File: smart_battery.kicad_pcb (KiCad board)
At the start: 4 copper layers, 50 x 18 mm, 98 parts, among them J101 Conn_01x02_Male, J102 Conn_01x02_Male, J103 Conn_01x05_Male, J104 Dronecode_Debug, Q101 RZM001P02T2L, Q201 PMGD280UN,115, Q202 PMGD280UN,115, U101 NCP716, U102 STM32F051K6Ux, U103 INA181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

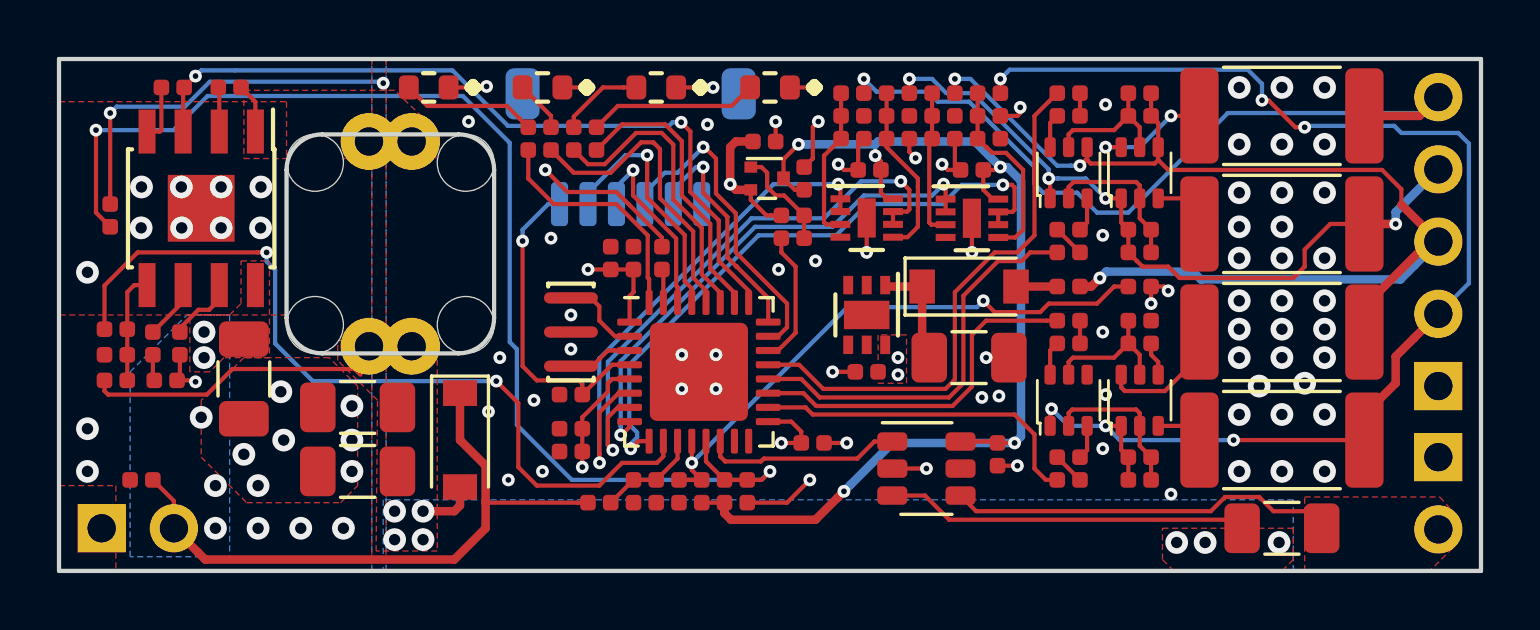
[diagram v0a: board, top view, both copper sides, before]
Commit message: Added some silkscreen
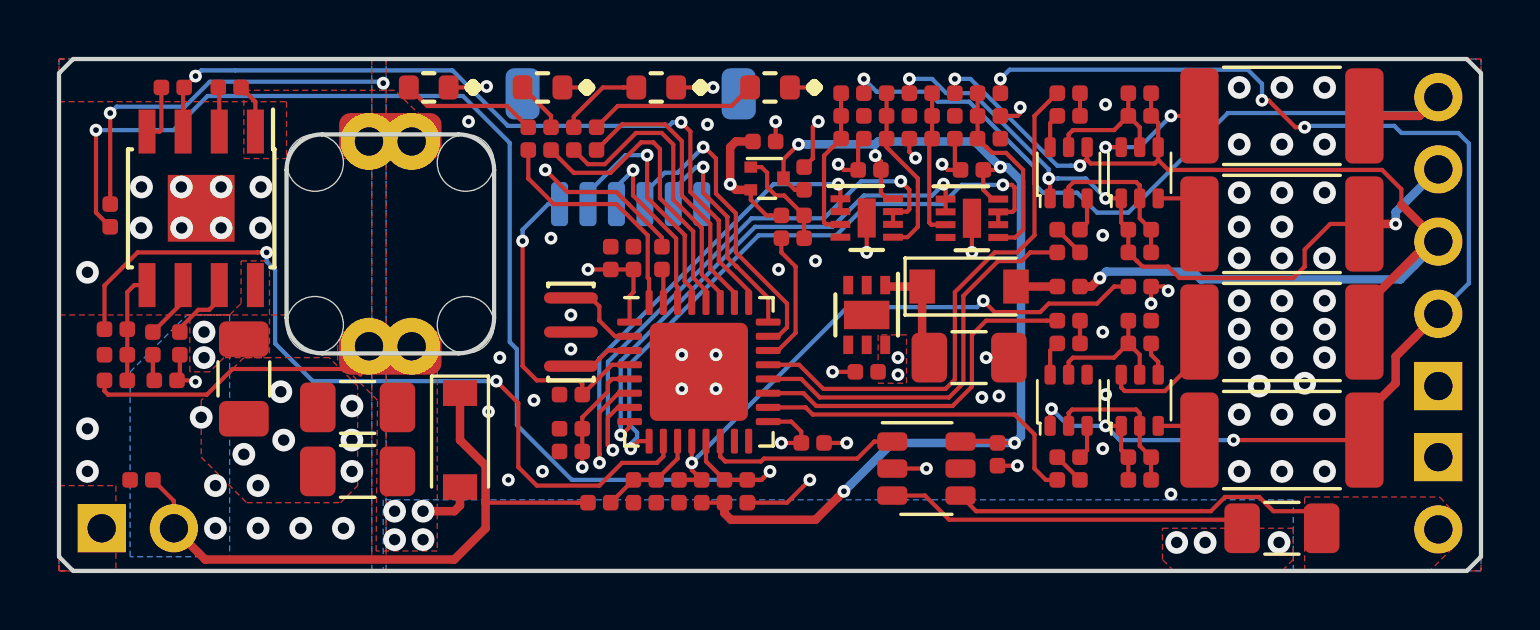
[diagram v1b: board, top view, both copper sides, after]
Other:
- outline, holes or cut-outs redrawn
- rule solder_mask_min_width: 0.09 -> 0.07
- board text added: "19V-24V"
- board text added: "BALANCE"
- board text added: "BAT"
- board text added: "BAT+"
- board text added: "BAT-"
- board text added: "CELL 1"
- board text added: "CELL 2"
- board text added: "CELL 3"
- board text added: "CELL 4"
- board text added: "CHG"
- board text added: "GND"
- board text added: "RST"
- board text added: "RX"
- board text added: "SWCLK"
- board text added: "SWDIO"
- board text added: "TX"

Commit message: Added button
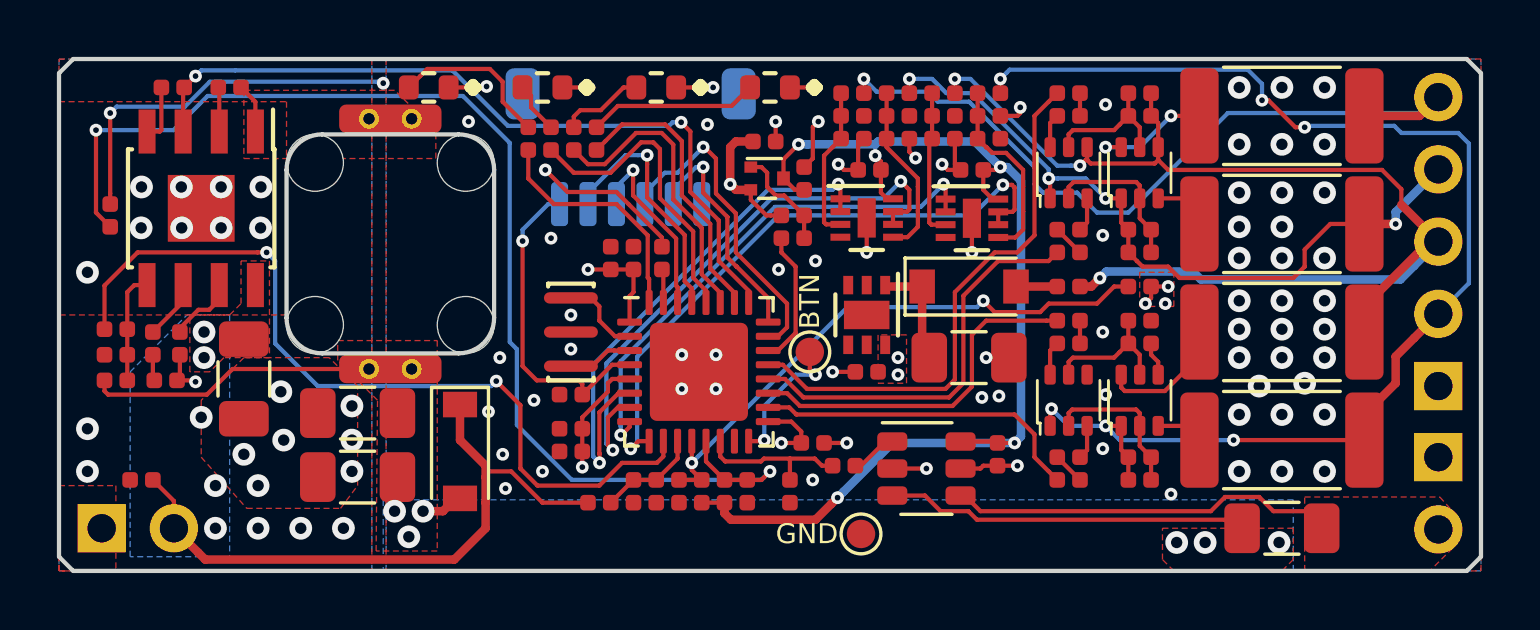
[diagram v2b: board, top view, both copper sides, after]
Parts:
- added C114: 0.1u, passive:C_0402_1005Metric_Rounded, F.Cu at (125.7, 95.2)
- added J105: Conn_01x01_Male, TestPoint:TestPoint_Pad_D1.0mm, F.Cu at (128.2, 96.7)
- added J106: Conn_01x01_Male, TestPoint:TestPoint_Pad_D1.0mm, F.Cu at (126.4, 90.3)
- added R113: 2.5k, passive:R_0402_1005Metric_Rounded, F.Cu at (127.6, 94.3)
- moved D301 0.40 mm to (114.1, 93.8)
- moved C305 0.20 mm to (110.5, 92.5)
- moved C306 0.20 mm to (110.5, 94.7)
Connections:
- U102 pad 16: Net-(U102-Pad16) -> /BTN
- U103 pad 1: /I_CHG -> Net-(R113-Pad2)
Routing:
- net /BTN: track 0.00 -> 4.90 mm, vias 0 -> 2
- net Net-(R113-Pad2): track 0.00 -> 1.65 mm
- net /I_CHG: track 6.95 -> 5.45 mm
- net GND: track 41.9 -> 40.7 mm, vias 77 -> 79
- net Net-(D102-Pad2): track 4.78 -> 5.73 mm
- net /buck_charger/OUT_CHARGER: track 24.8 -> 24.3 mm, vias 7 -> 6
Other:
- board text added: "BTN"
- board text added: "Smart Battery v1.0 By Emil Fresk"
